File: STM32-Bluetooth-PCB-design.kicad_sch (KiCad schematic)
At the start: 0 parts

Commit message: Connected power sources, grounds and the high and low speed external oscillators
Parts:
- added C1, C7: 4u7, symbol Device:C
- added C10, C2, C3, C4, C5, C6, C8: 100n, symbol Device:C
- added U1: STM32WB55CEU6, Package_DFN_QFN:QFN-48-1EP_7x7mm_P0.5mm_EP5.6x5.6mm, symbol MCU_ST_STM32WB:STM32WB55CEUx
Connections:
- new net +3.3V: C1.1, C10.1, C2.1, C3.1, C4.1, C5.1, C6.1, C7.1, C8.1, U1.1 (VBAT), U1.20 (VDD), U1.23 (VDDRF), U1.34 (VDDSMPS), U1.35 (VDD), U1.40 (VDDUSB), U1.48 (VDD), U1.8 (VDDA)
- new net GND: C1.2, C10.2, C2.2, C3.2, C4.2, C5.2, C6.2, C7.2, C8.2, U1.22 (VSSRF), U1.32 (VSSSMPS), U1.49 (VSS)

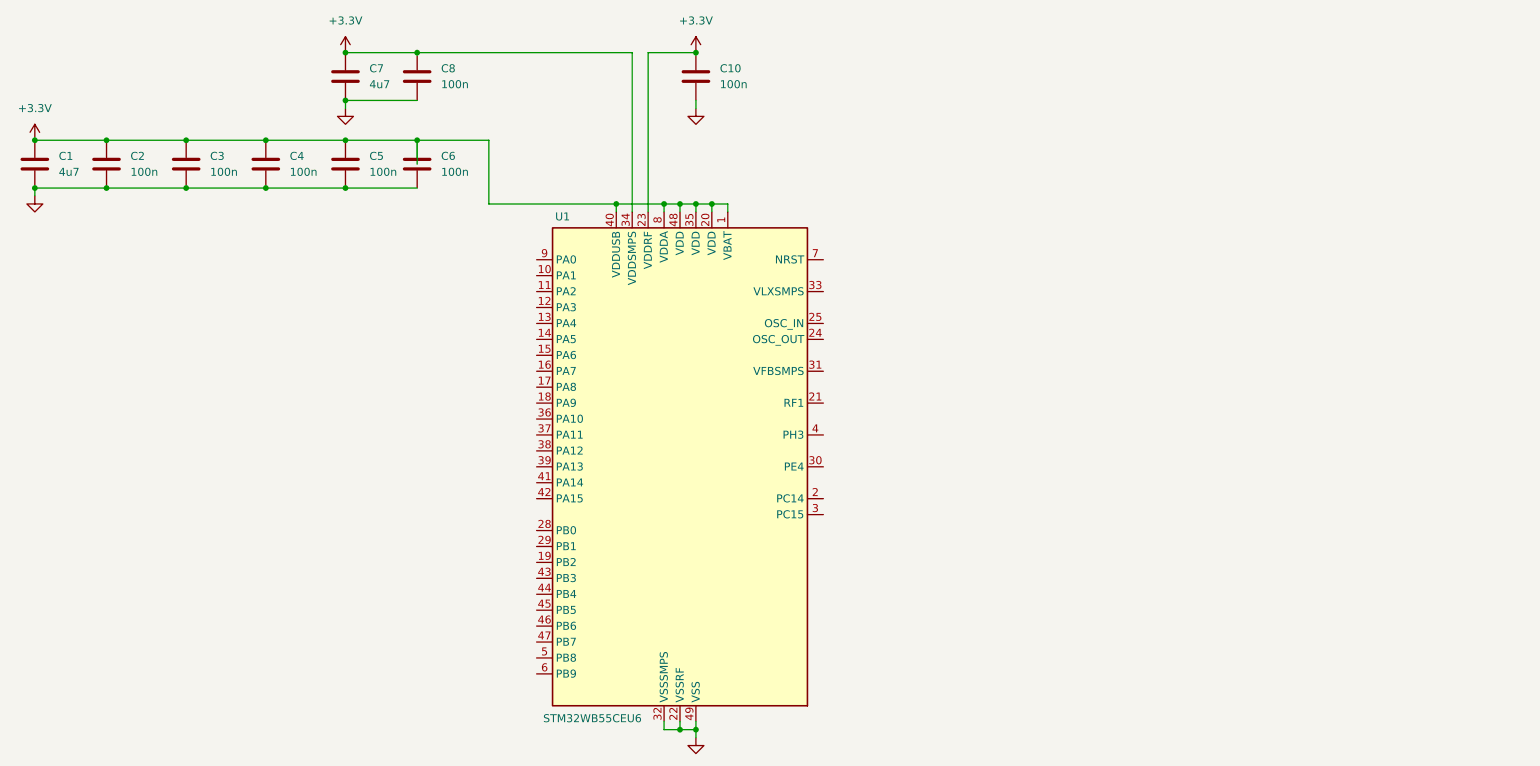
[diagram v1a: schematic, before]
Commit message: Created schematic for LPF recommended by manufacturer for RF section, as well as 50 ohm matching network connected to a coaxial cable connector
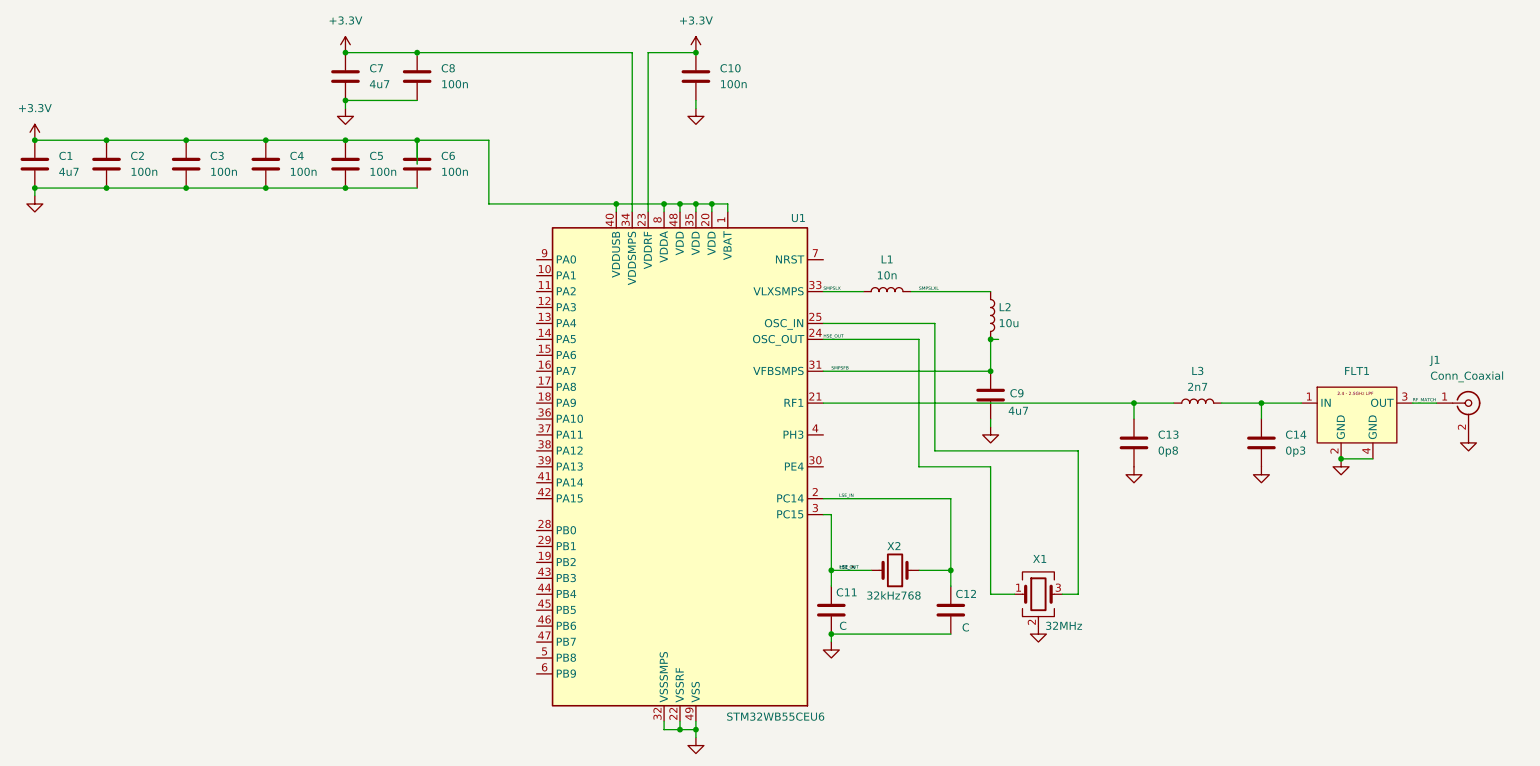
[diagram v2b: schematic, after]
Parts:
- added C11, C12: C, symbol Device:C
- added C13: 0p8, symbol Device:C
- added C14: 0p3, symbol Device:C
- added C9: 4u7, symbol Device:C
- added FLT1: (no value), Bluetooth MCU PCB design:DLF162500LT-5028A1, symbol Bluetooth MCU PCB design:DLF162500LT-5028A1
- added J1: Conn_Coaxial, symbol Connector:Conn_Coaxial
- added L1: 10n, symbol Device:L
- added L2: 10u, symbol Device:L
- added L3: 2n7, symbol Device:L
- added X1: 32MHz, symbol Device:Crystal_GND24
- added X2: 32kHz768, symbol Device:Crystal
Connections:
- net GND: now also C11.2, C12.2, C13.2, C14.2, C9.2, FLT1.2 (GND), FLT1.4 (GND), J1.2 (Ext), X1.2 (G), X1.4 (G)
- net LSE_IN: now reaches U1.2 (PC14)
- net LSE_IN: now also C12.1, X2.1
- net at U1.21 (RF1): now also C13.1, L3.1
- net HSE_OUT: now reaches U1.24 (OSC_OUT)
- net HSE_OUT: now also X1.1
- net at U1.25 (OSC_IN): now also X1.3
- net HSE_IN: now reaches U1.3 (PC15)
- net HSE_IN: now also C11.1, X2.2
- net SMPSFB: now reaches U1.31 (VFBSMPS)
- net SMPSFB: now also C9.1, L2.2
- net SMPSLX: now reaches U1.33 (VLXSMPS)
- net SMPSLX: now also L1.1
- new net: C14.1, FLT1.1 (IN), L3.2
- new net RF_MATCH: FLT1.3 (OUT), J1.1 (In)
- new net SMPSLXL: L1.2, L2.1
